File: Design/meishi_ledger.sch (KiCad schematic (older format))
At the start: 0 parts

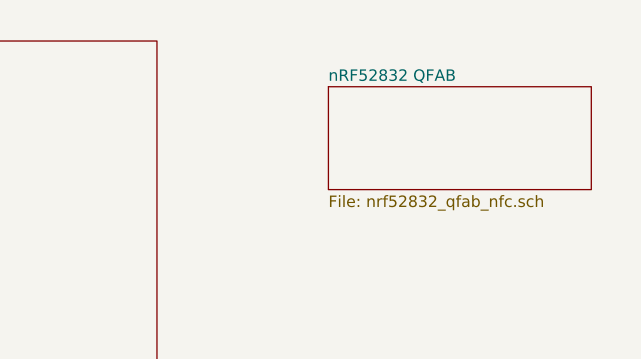
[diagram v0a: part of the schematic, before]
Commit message: Improvement over the Power management: - added TPS6201DRC for raising leaking voltage from supercapacitor - supercap is protected from overvoltage using a shunt diode - power management is using MOSFET logic (2 PFET, 1 NFET)
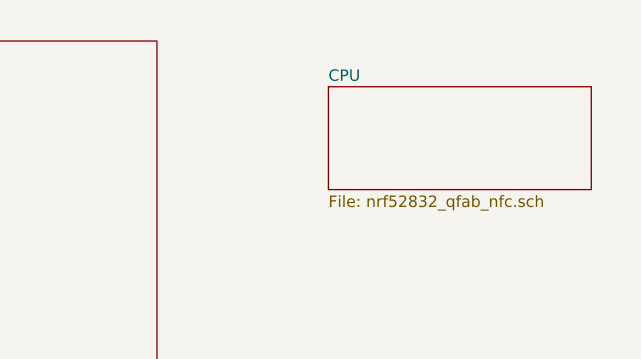
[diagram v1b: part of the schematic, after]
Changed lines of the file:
@@
 S 9500 1300 1150 450
 U 5E12FBFF
-F0 "nRF52832 QFAB" 50
+F0 "CPU" 50
 F1 "nrf52832_qfab_nfc.sch" 50
 $EndSheet

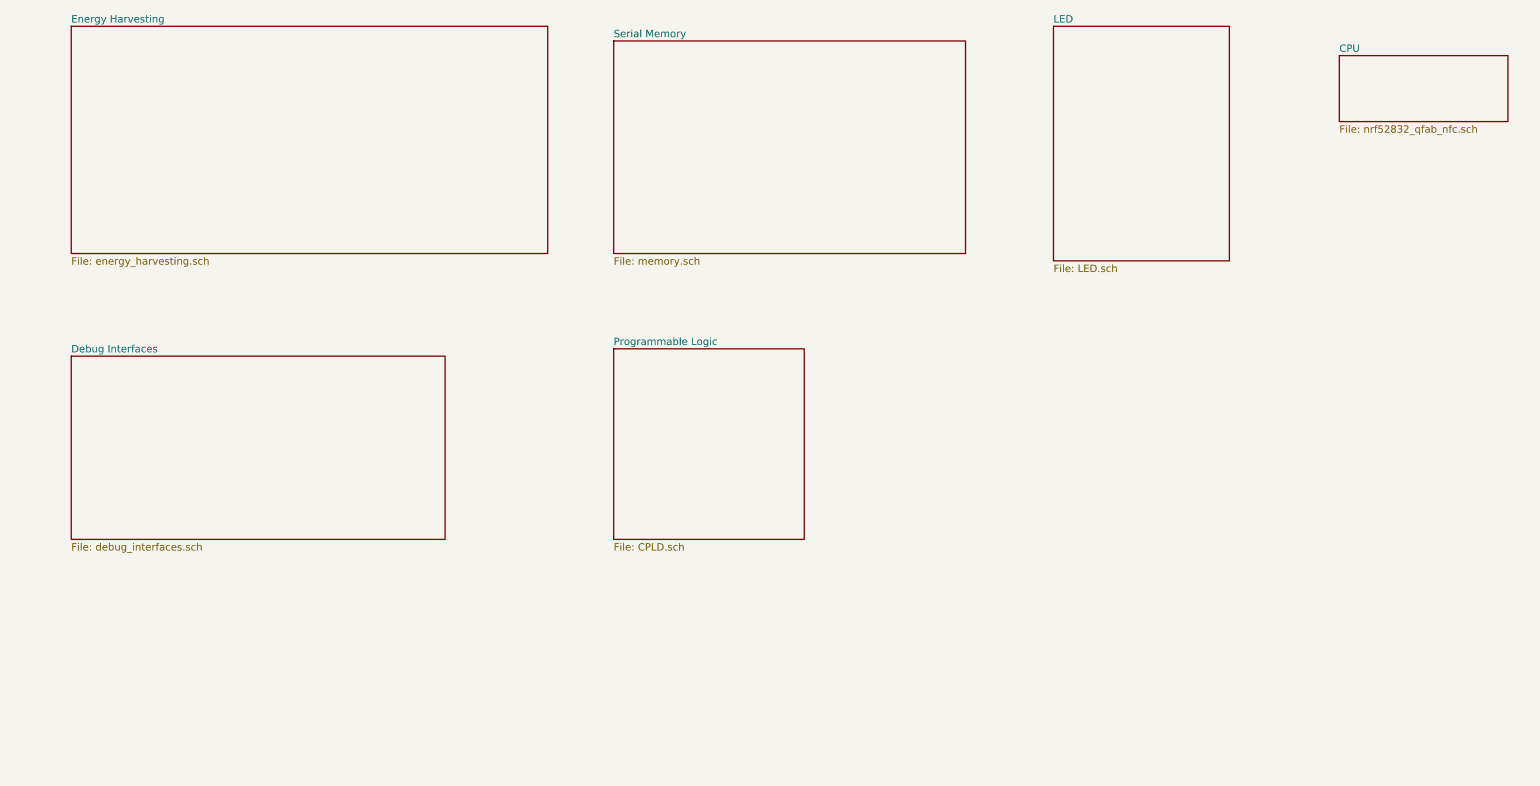
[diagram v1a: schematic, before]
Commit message: - designed configurable intensity for RGB LEDs - included Breakout (FET, Diode, etc.) Spice models from Cadence Spice - replaced global label with hierarchical complete view - customized net labels with pin function - exported first spice netlist which presents small bugs
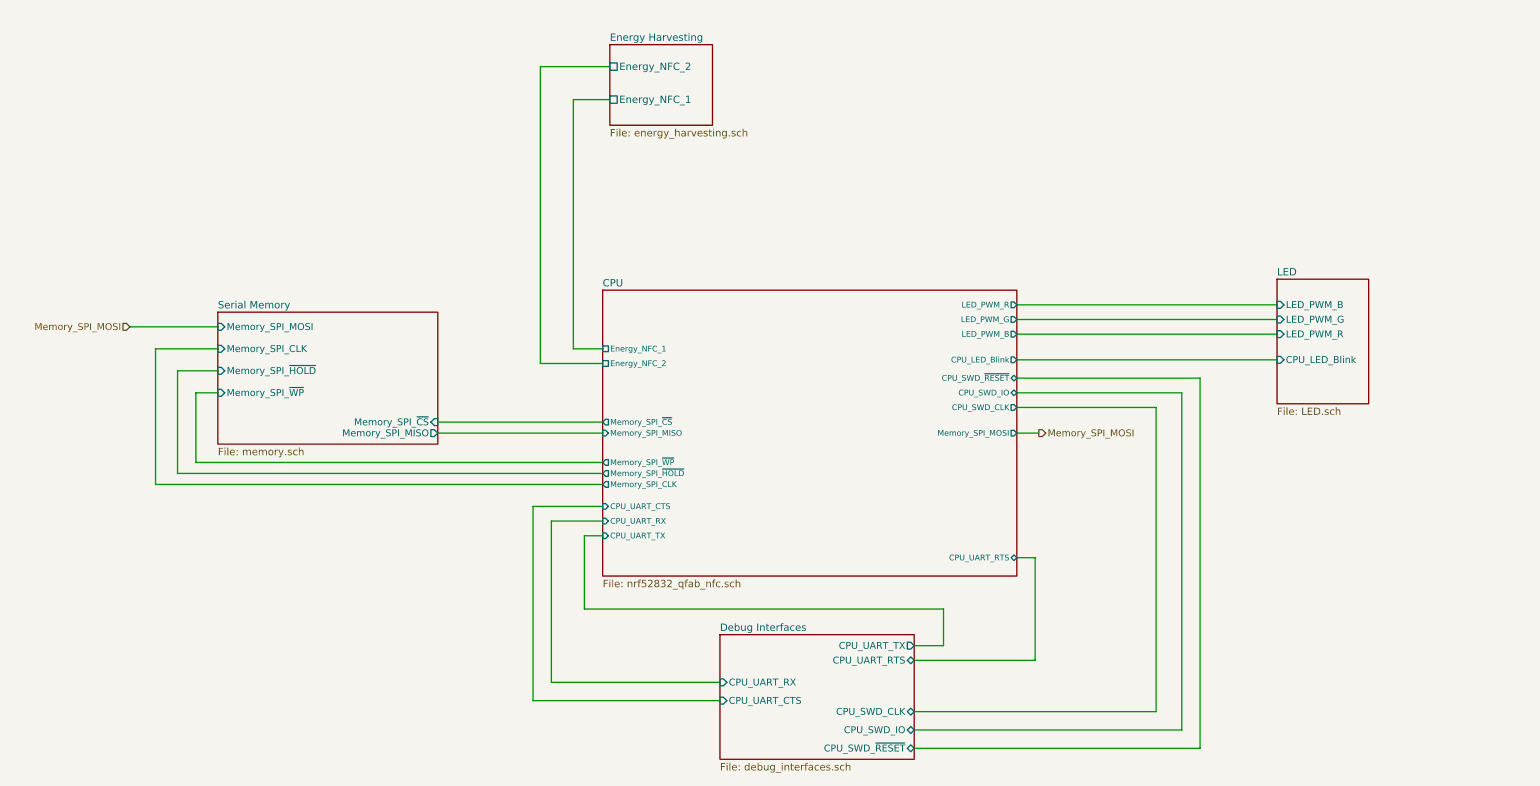
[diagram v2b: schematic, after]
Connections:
- net labels added: Memory_SPI_MOSI
- wire segments 0 -> 46
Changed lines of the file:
@@
 $Descr A4 11693 8268
 encoding utf-8
-Sheet 1 7
+Sheet 1 6
 Title "meishi_ledger.sch"
-Date "2020-01-01"
+Date "2019-12-13"
 Rev "1.0A"
-Comp "Meishi Corporation"
-Comment1 ""
-Comment2 ""
-Comment3 ""
-Comment4 ""
+Comp "Meishi Smart Luxury"
+Comment1 "Author: Steve Huguenin-Elie"
+Comment2 "Espace de l'Europe"
+Comment3 "2000 Neuchâtel"
+Comment4 "Switzerland, CH"
 $EndDescr
 $Sheet
-S 850  1100 3250 1550
+S 9075 2825 625  850
+U 5E12D0D3
+F0 "LED" 50
+F1 "LED.sch" 50
+F2 "CPU_LED_Blink" I L 9075 3375 47
+F3 "LED_PWM_B" I L 9075 3000 47
+F4 "LED_PWM_G" I L 9075 3100 47
+F5 "LED_PWM_R" I L 9075 3200 47
+$EndSheet
+$Sheet
+S 1850 3050 1500 900
+U 5E12BE09
+F0 "Serial Memory" 50
+F1 "memory.sch" 50
+F2 "Memory_SPI_MOSI" I L 1850 3150 47
+F3 "Memory_SPI_CLK" I L 1850 3300 47
+F4 "Memory_SPI_~CS~" I R 3350 3800 47
+F5 "Memory_SPI_~WP~" I L 1850 3600 47
+F6 "Memory_SPI_~HOLD~" I L 1850 3450 47
+F7 "Memory_SPI_MISO" O R 3350 3875 47
+$EndSheet
+Wire Wire Line
+	4275 3300 4475 3300
+$Sheet
+S 4524 1225 700  550
 U 5E12BC63
 F0 "Energy Harvesting" 50
 F1 "energy_harvesting.sch" 50
+F2 "Energy_NFC_1" U L 4524 1600 50
+F3 "Energy_NFC_2" U L 4524 1375 50
 $EndSheet
+Wire Wire Line
+	4525 1600 4275 1600
+Wire Wire Line
+	4275 1600 4275 3300
+Wire Wire Line
+	4525 1375 4050 1375
+Wire Wire Line
+	4050 1375 4050 3400
+Wire Wire Line
+	4050 3400 4475 3400
+Wire Wire Line
+	3350 3875 4475 3875
+Wire Wire Line
+	7300 3000 9075 3000
+Wire Wire Line
+	7300 3200 9075 3200
+Wire Wire Line
+	7300 3100 9075 3100
+Wire Wire Line
+	7300 3375 9075 3375
+Wire Wire Line
+	7300 3600 8425 3600
+Wire Wire Line
+	8425 3600 8425 5900
+Wire Wire Line
+	8425 5900 6600 5900
+Wire Wire Line
+	7300 3700 8250 3700
+Wire Wire Line
+	8250 3700 8250 5775
+Wire Wire Line
+	8250 5775 6600 5775
+Wire Wire Line
+	4350 4575 4475 4575
+Wire Wire Line
+	5275 5575 4125 5575
+Wire Wire Line
+	4125 5575 4125 4475
+Wire Wire Line
+	4125 4475 4475 4475
+Wire Wire Line
+	5275 5700 4000 5700
+Wire Wire Line
+	4000 5700 4000 4375
+Wire Wire Line
+	4000 4375 4475 4375
 $Sheet
-S 7550 1100 1200 1600
-U 5E12D0D3
-F0 "LED" 50
-F1 "LED.sch" 50
-$EndSheet
-$Sheet
-S 9500 1300 1150 450
+S 4475 2900 2825 1950
 U 5E12FBFF
 F0 "CPU" 50
 F1 "nrf52832_qfab_nfc.sch" 50
+F2 "LED_PWM_R" O R 7300 3000 39
+F3 "LED_PWM_G" O R 7300 3100 39
+F4 "LED_PWM_B" O R 7300 3200 39
+F5 "Energy_NFC_2" U L 4475 3400 39
+F6 "Energy_NFC_1" U L 4475 3300 39
+F7 "CPU_LED_Blink" O R 7300 3375 39
+F8 "CPU_SWD_IO" B R 7300 3600 39
+F9 "CPU_SWD_CLK" O R 7300 3700 39
+F10 "Memory_SPI_MISO" I L 4475 3875 39
+F11 "Memory_SPI_MOSI" O R 7300 3875 39
+F12 "Memory_SPI_~CS~" O L 4475 3800 39
+F13 "Memory_SPI_~WP~" O L 4475 4075 39
+F14 "Memory_SPI_~HOLD~" O L 4475 4150 39
+F15 "Memory_SPI_CLK" O L 4475 4225 39
+F16 "CPU_UART_RTS" B R 7300 4725 39
+F17 "CPU_UART_TX" I L 4475 4575 39
+F18 "CPU_UART_RX" I L 4475 4475 39
+F19 "CPU_UART_CTS" I L 4475 4375 39
+F20 "CPU_SWD_~RESET~" B R 7300 3500 39
 $EndSheet
+Wire Wire Line
+	7300 3500 8550 3500
+Wire Wire Line
+	8550 6025 6600 6025
+Wire Wire Line
+	8550 3500 8550 6025
 $Sheet
-S 4550 1200 2400 1450
-U 5E12BE09
-F0 "Serial Memory" 50
-F1 "memory.sch" 50
-$EndSheet
-$Sheet
-S 850  3350 2550 1250
+S 5275 5250 1325 850
 U 5E155A40
 F0 "Debug Interfaces" 50
 F1 "debug_interfaces.sch" 50
+F2 "CPU_UART_RTS" B R 6600 5425 47
+F3 "CPU_UART_TX" O R 6600 5325 47
+F4 "CPU_UART_RX" I L 5275 5575 47
+F5 "CPU_UART_CTS" I L 5275 5700 47
+F6 "CPU_SWD_~RESET~" B R 6600 6025 47
+F7 "CPU_SWD_CLK" B R 6600 5775 47
+F8 "CPU_SWD_IO" B R 6600 5900 47
 $EndSheet
-$Sheet
-S 4550 3300 1300 1300
-U 5E1FD901
-F0 "Programmable Logic" 50
-F1 "CPLD.sch" 50
-$EndSheet
+Wire Wire Line
+	4350 4575 4350 5075
+Wire Wire Line
+	6600 5425 7425 5425
+Wire Wire Line
+	7425 5425 7425 4725
+Wire Wire Line
+	7425 4725 7300 4725
+Wire Wire Line
+	6800 5325 6600 5325
+Wire Wire Line
+	4350 5075 6800 5075
+Wire Wire Line
+	6800 5075 6800 5325
+Wire Wire Line
+	4475 4225 1425 4225
+Wire Wire Line
+	1425 4225 1425 3300
+Wire Wire Line
+	1425 3300 1850 3300
+Wire Wire Line
+	1850 3450 1575 3450
+Wire Wire Line
+	1575 3450 1575 4150
+Wire Wire Line
+	1575 4150 4475 4150
+Wire Wire Line
+	4475 4075 1700 4075
+Wire Wire Line
+	1700 4075 1700 3600
+Wire Wire Line
+	1700 3600 1850 3600
+Wire Wire Line
+	3350 3800 4475 3800
+Text HLabel 1250 3150 0    47   Input ~ 0
+Memory_SPI_MOSI
+Wire Wire Line
+	1250 3150 1850 3150
+Text HLabel 7450 3875 2    47   Output ~ 0
+Memory_SPI_MOSI
+Wire Wire Line
+	7450 3875 7300 3875
 $EndSCHEMATC
